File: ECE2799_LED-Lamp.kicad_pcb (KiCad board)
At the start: 2 copper layers, 138 x 46 mm, 91 parts, among them J1 IEC_60320_C8_Receptacle, J4 Conn_01x32, T1 750817251, U1 LT3799EMSE-PBF, U2 MP9989GV-Z, U3 LMR36006BRNXT, U4 FDMQ8205A, U5 140356145400, U6 140356145400, U7 RP2040, U8 CY8C20666A-24LQXI

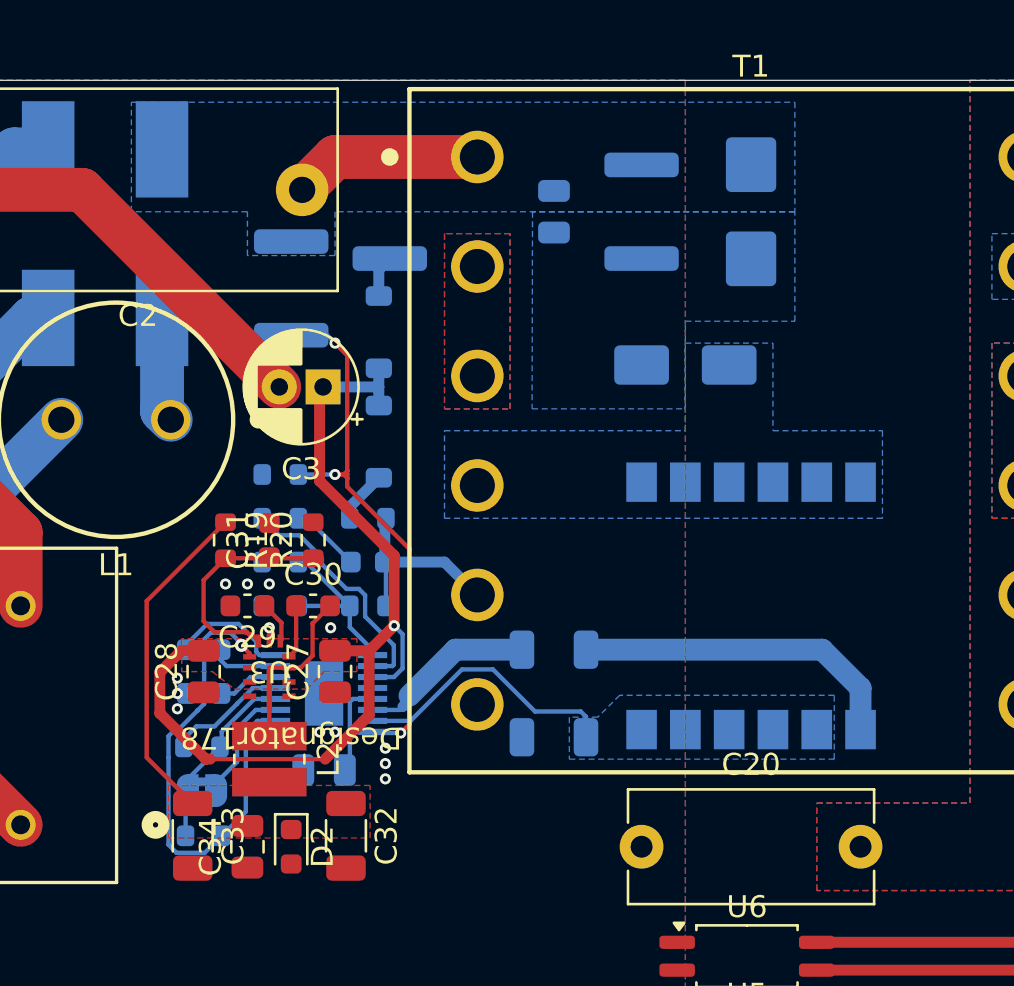
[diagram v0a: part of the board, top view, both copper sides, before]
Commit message: new FET
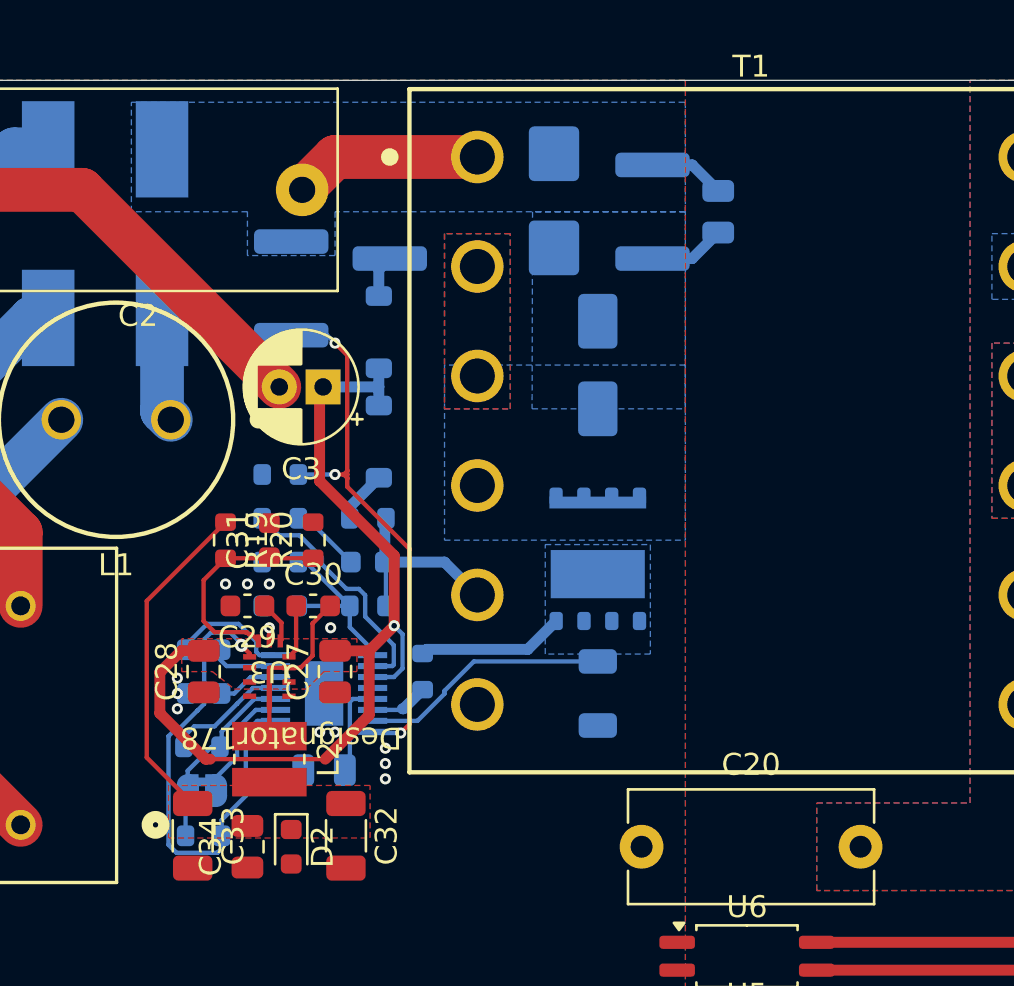
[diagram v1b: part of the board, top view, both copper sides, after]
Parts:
- C12, C14, C15, C16, C17: value C -> 100n
- C5: value C -> 1u
- Q1: value ~ -> IGLR65R200D2; footprint GAN039-650NTB:GAN039-650NTB -> PG-TSON-8-8:PG-TSON-8-8
- R25: footprint Resistor_SMD:R_1206_3216Metric -> Resistor_SMD:R_0603_1608Metric
- moved D3 9.01 mm to (151.0, 89.5)
- moved C13 7.50 mm to (158.5, 90.0)
- moved Q1 7.32 mm to (153.0, 105.8), turned to 90 degrees
- moved R25 6.08 mm to (145.0, 111.0), turned to 90 degrees
- moved D4 4.00 mm to (153.0, 97.0), turned to -90 degrees
- moved R8 2.83 mm to (153.0, 112.0), turned to -90 degrees
- moved R32 0.50 mm to (155.5, 90.0)
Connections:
- Q1 pad 1: /LED_Driver_AC-DC/GATE -> /LED_Driver_AC-DC/SENSE
- Q1 pad 4: /LED_Driver_AC-DC/SENSE -> /LED_Driver_AC-DC/GATE
- Q1 pad 5: /LED_Driver_AC-DC/SENSE -> /LED_Driver_AC-DC/DRAIN
- Q1 pad 6: /LED_Driver_AC-DC/SENSE -> /LED_Driver_AC-DC/DRAIN
- Q1 pad 9: /LED_Driver_AC-DC/DRAIN -> /LED_Driver_AC-DC/SENSE
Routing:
- net /LED_Driver_AC-DC/GATE: track 15.2 -> 6.72 mm
- net Net-(U1-GATE): track 8.08 -> 2.65 mm
- net /LED_Driver_AC-DC/FREEWHEEL: track 0.00 -> 3.49 mm
- net /LED_Driver_AC-DC/VHV: track 8.62 -> 12.1 mm
- net /LED_Driver_AC-DC/SENSE: track 12.6 -> 11.5 mm

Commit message: touch pcb
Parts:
- removed J4: Conn_01x32, Connector_FFC-FPC:Hirose_FH12-32S-0.5SH_1x32-1MP_P0.50mm_Horizontal
- added CS1: TRILL_BAR-26_CapSense, TRILL:TRILL_BAR_CapSense, F.Cu at (146.0, 140.0)
- added G5: OpenSourceHardware_Logo, TRILL:OpenSourceHardware_Logo, F.Cu at (95.5, 160.0)
- added J2: Conn_01x04_MountingPin, TRILL:qwiic_horizontal_SMD, B.Cu at (208.0, 145.0)
- moved C18 43.6 mm to (200.0, 138.0), turned to -90 degrees
- moved U8 41.1 mm to (200.0, 144.0)
- moved U7 0.40 mm to (217.0, 93.0), turned to 90 degrees
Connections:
- U8 pad 10: /Capacitive_Touch_Sensor/SENSE26 -> /Capacitive_Touch_Sensor/SENSE22
- U8 pad 11: /Capacitive_Touch_Sensor/SENSE27 -> /Capacitive_Touch_Sensor/SENSE23
- U8 pad 12: /Capacitive_Touch_Sensor/SENSE28 -> /Capacitive_Touch_Sensor/SENSE24
- U8 pad 13: /Capacitive_Touch_Sensor/SENSE29 -> /Capacitive_Touch_Sensor/SENSE25
- U8 pad 16: /Capacitive_Touch_Sensor/SENSE30 -> /Capacitive_Touch_Sensor/SENSE26
- U8 pad 2: /Capacitive_Touch_Sensor/SENSE18 -> unconnected-(U8-P2[7]-Pad2)
- U8 pad 3: /Capacitive_Touch_Sensor/SENSE19 -> unconnected-(U8-P2[5]-Pad3)
- U8 pad 4: /Capacitive_Touch_Sensor/SENSE20 -> unconnected-(U8-P2[3]-Pad4)
- U8 pad 5: /Capacitive_Touch_Sensor/SENSE21 -> unconnected-(U8-P2[1]-Pad5)
- U8 pad 6: /Capacitive_Touch_Sensor/SENSE22 -> /Capacitive_Touch_Sensor/SENSE18
- U8 pad 7: /Capacitive_Touch_Sensor/SENSE23 -> /Capacitive_Touch_Sensor/SENSE19
- U8 pad 8: /Capacitive_Touch_Sensor/SENSE24 -> /Capacitive_Touch_Sensor/SENSE20
- U8 pad 9: /Capacitive_Touch_Sensor/SENSE25 -> /Capacitive_Touch_Sensor/SENSE21
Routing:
- net /Capacitive_Touch_Sensor/SENSE1: track 0.00 -> 112.3 mm, vias 0 -> 1
- net /Capacitive_Touch_Sensor/SENSE2: track 0.00 -> 108.1 mm, vias 0 -> 1
- net /Capacitive_Touch_Sensor/SENSE3: track 0.00 -> 104.0 mm, vias 0 -> 1
- net /Capacitive_Touch_Sensor/SENSE4: track 0.00 -> 99.9 mm, vias 0 -> 1
- net /Capacitive_Touch_Sensor/SENSE5: track 0.00 -> 95.7 mm, vias 0 -> 1
- net /Capacitive_Touch_Sensor/SENSE6: track 0.00 -> 91.6 mm, vias 0 -> 1
- net /Capacitive_Touch_Sensor/SENSE7: track 0.00 -> 87.5 mm, vias 0 -> 1
- net /Capacitive_Touch_Sensor/SENSE8: track 0.00 -> 83.6 mm, vias 0 -> 1
- net /Capacitive_Touch_Sensor/SENSE9: track 0.00 -> 79.5 mm, vias 0 -> 1
- net /Capacitive_Touch_Sensor/SENSE10: track 0.00 -> 75.4 mm, vias 0 -> 1
- net /Capacitive_Touch_Sensor/SENSE11: track 0.00 -> 74.1 mm, vias 0 -> 1
- net /Capacitive_Touch_Sensor/SENSE12: track 0.00 -> 70.9 mm, vias 0 -> 1
- net /Capacitive_Touch_Sensor/SENSE13: track 0.00 -> 67.5 mm, vias 0 -> 1
- net /Capacitive_Touch_Sensor/SENSE14: track 0.00 -> 64.0 mm, vias 0 -> 1
- net /Capacitive_Touch_Sensor/SENSE15: track 0.00 -> 61.0 mm, vias 0 -> 1
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- added copper zone on B.Cu, net /Capacitive_Touch_Sensor/SENSE1
- added copper zone on B.Cu, net /Capacitive_Touch_Sensor/SENSE10
- added copper zone on B.Cu, net /Capacitive_Touch_Sensor/SENSE11
- added copper zone on B.Cu, net /Capacitive_Touch_Sensor/SENSE12
- added copper zone on B.Cu, net /Capacitive_Touch_Sensor/SENSE13
- added copper zone on B.Cu, net /Capacitive_Touch_Sensor/SENSE14
- added copper zone on B.Cu, net /Capacitive_Touch_Sensor/SENSE15
- added copper zone on B.Cu, net /Capacitive_Touch_Sensor/SENSE16
- added copper zone on B.Cu, net /Capacitive_Touch_Sensor/SENSE17
- added copper zone on B.Cu, net /Capacitive_Touch_Sensor/SENSE18
- added copper zone on B.Cu, net /Capacitive_Touch_Sensor/SENSE19
- added copper zone on B.Cu, net /Capacitive_Touch_Sensor/SENSE2
- added copper zone on B.Cu, net /Capacitive_Touch_Sensor/SENSE20
- added copper zone on B.Cu, net /Capacitive_Touch_Sensor/SENSE21
- added copper zone on B.Cu, net /Capacitive_Touch_Sensor/SENSE22
- added copper zone on B.Cu, net /Capacitive_Touch_Sensor/SENSE23
- added copper zone on B.Cu, net /Capacitive_Touch_Sensor/SENSE24
- added copper zone on B.Cu, net /Capacitive_Touch_Sensor/SENSE25
- added copper zone on B.Cu, net /Capacitive_Touch_Sensor/SENSE26
- added copper zone on B.Cu, net /Capacitive_Touch_Sensor/SENSE3
- added copper zone on B.Cu, net /Capacitive_Touch_Sensor/SENSE4
- added copper zone on B.Cu, net /Capacitive_Touch_Sensor/SENSE5
- added copper zone on B.Cu, net /Capacitive_Touch_Sensor/SENSE6
- added copper zone on B.Cu, net /Capacitive_Touch_Sensor/SENSE7
- added copper zone on B.Cu, net /Capacitive_Touch_Sensor/SENSE8
- added copper zone on B.Cu, net /Capacitive_Touch_Sensor/SENSE9
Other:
- board size 138 x 46 mm -> 116 x 72 mm

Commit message: updated components
New ganfet selected and further work developing the rp2040 microcontroller circuit
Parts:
- removed H1: MountingHole_Pad, MountingHole:MountingHole_3.2mm_M3_Pad
- added C22: 100n, Capacitor_SMD:C_0603_1608Metric, F.Cu at (234.2, 90.0)
- added C24: 100n, Capacitor_SMD:C_0603_1608Metric, F.Cu at (234.2, 92.5)
- added C25: 100n, Capacitor_SMD:C_0603_1608Metric, F.Cu at (234.2, 95.0)
- added C26: 33p, Capacitor_SMD:C_0603_1608Metric, F.Cu at (215.7, 70.4)
- added C35: 33p, Capacitor_SMD:C_0603_1608Metric, F.Cu at (215.7, 72.9)
- added C36: C, Capacitor_SMD:C_0603_1608Metric, F.Cu at (215.7, 75.4)
- added C37: C, Capacitor_SMD:C_0603_1608Metric, F.Cu at (215.7, 77.9)
- added J3: Conn_ARM_SWD_TagConnect_TC2030-NL, Connector:Tag-Connect_TC2030-IDC-NL_2x03_P1.27mm_Vertical, F.Cu at (228.2, 91.2)
- added J4: Conn_01x02_Pin, Connector_PinHeader_2.54mm:PinHeader_1x02_P2.54mm_Vertical, F.Cu at (250.0, 97.5)
- added J5: Conn_01x04_MountingPin, TRILL:qwiic_horizontal_SMD, F.Cu at (241.2, 100.2)
- added JP1: SolderJumper_2_Bridged, Jumper:SolderJumper-2_P1.3mm_Bridged2Bar_RoundedPad1.0x1.5mm, F.Cu at (227.8, 79.0)
- added R28: 0, Resistor_SMD:R_0603_1608Metric, F.Cu at (215.7, 80.4)
- added R29: 1k, Resistor_SMD:R_0603_1608Metric, F.Cu at (215.7, 82.9)
- added R30: 100, Resistor_SMD:R_0603_1608Metric, F.Cu at (219.7, 70.4)
- added R31: 100, Resistor_SMD:R_0603_1608Metric, F.Cu at (219.7, 72.9)
- added R33: 1k, Resistor_SMD:R_0603_1608Metric, F.Cu at (219.7, 75.4)
- added R34: 27.4, Resistor_SMD:R_0603_1608Metric, F.Cu at (219.7, 77.9)
- added R35: 27.4, Resistor_SMD:R_0603_1608Metric, F.Cu at (219.7, 80.4)
- added R36: R, Resistor_SMD:R_0603_1608Metric, F.Cu at (219.7, 82.9)
- added R37: R, Resistor_SMD:R_0603_1608Metric, F.Cu at (223.7, 70.4)
- added R38: R, Resistor_SMD:R_0603_1608Metric, F.Cu at (223.7, 72.9)
- added R39: 4.7k, Resistor_SMD:R_0603_1608Metric, F.Cu at (223.7, 75.4)
- added R40: 4.7k, Resistor_SMD:R_0603_1608Metric, F.Cu at (223.7, 77.9)
- added TP1: TestPoint, TestPoint:TestPoint_Pad_D2.0mm, F.Cu at (227.7, 71.2)
- added TP2: TestPoint, TestPoint:TestPoint_Pad_D2.0mm, F.Cu at (227.7, 75.2)
- added U9: AT25xxx, Package_SO:SOIC-8_3.9x4.9mm_P1.27mm, F.Cu at (228.4, 85.5)
- added Y1: 830070868, Crystal:Crystal_SMD_3225-4Pin_3.2x2.5mm, F.Cu at (235.2, 84.4)
- C15: value 100n -> 1u
- J1: value IEC_60320_C8_Receptacle -> IEC_60320_C6_Receptacle; footprint RAPC322X:SWITCHCRAFT_RAPC322X -> IEC_60320_C6:IEC_60320_C6
- J2: moved to F.Cu
- moved G5 98.8 mm to (193.0, 144.0)
- moved C19 50.9 mm to (202.0, 150.0), turned to 180 degrees
- moved R21 48.9 mm to (208.0, 149.0), turned to 0 degrees
- moved R17 39.7 mm to (208.0, 139.0), turned to 0 degrees
- moved JP3 38.2 mm to (207.0, 135.0), turned to 90 degrees
- moved RV1 36.9 mm to (106.8, 124.5), turned to 180 degrees
- moved JP4 33.3 mm to (210.0, 135.0), turned to 90 degrees
- moved R22 32.4 mm to (205.0, 134.0), turned to 90 degrees
- moved R24 26.6 mm to (212.0, 134.0), turned to 90 degrees
- moved J1 9.85 mm to (94.0, 107.0)
- moved J2 2.60 mm to (210.4, 144.0), turned to 90 degrees
- moved FL1 1.85 mm to (128.5, 118.0)
- moved C1 1.50 mm to (113.5, 100.0)
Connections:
- net Net-(U7-VREG_VOUT) renamed +1V1
- C18 pad 1: GND -> GND1
- C18 pad 2: +3V3 -> VCC
- C19 pad 2: GND -> GND1
- C2 pad 2: GND -> GNDPWR
- C20 pad 1: GND -> GNDPWR
- C27 pad 1: GND -> GNDPWR
- C28 pad 1: GND -> GNDPWR
- C29 pad 2: GND -> GNDPWR
- C3 pad 2: GND -> GNDPWR
- C31 pad 2: GND -> GNDPWR
- C32 pad 2: GND -> GNDPWR
- C33 pad 2: GND -> GNDPWR
- C34 pad 1: GND -> GNDPWR
- C7 pad 2: GND -> GNDPWR
- C8 pad 1: GND -> GNDPWR
- C9 pad 1: GND -> GNDPWR
- D1 pad 4: GND -> GNDPWR
- D2 pad 2: GND -> GNDPWR
- J2 pad 1: GND -> GND1
- J2 pad 2: +3V3 -> VCC
- J2 pad MP: GND -> GND1
- JP3 pad 1: +3V3 -> VCC
- JP3 pad 3: GND -> GND1
- JP4 pad 1: unconnected-(JP4-A-Pad1) -> VCC
- JP4 pad 3: GND -> GND1
- R20 pad 2: GND -> GNDPWR
- R22 pad 2: GND -> GND1
- R23 pad 2: GND -> GNDPWR
- R24 pad 2: GND -> GND1
- R4 pad 1: GND -> GNDPWR
- R8 pad 2: GND -> GNDPWR
- T1 pad 6: GND -> GNDPWR
- U1 pad EPAD: GND -> GNDPWR
- U3 pad 1: GND -> GNDPWR
- U3 pad 11: GND -> GNDPWR
- U3 pad 6: GND -> GNDPWR
- U7 pad 19: unconnected-(U7-TESTEN-Pad19) -> GND
- U7 pad 2: unconnected-(U7-GPIO0-Pad2) -> /Microcontroller/SDA
- U7 pad 20: unconnected-(U7-XIN-Pad20) -> /Microcontroller/XIN
- U7 pad 21: unconnected-(U7-XOUT-Pad21) -> /Microcontroller/XOUT
- U7 pad 24: unconnected-(U7-SWCLK-Pad24) -> /Microcontroller/SWCLK
- U7 pad 25: unconnected-(U7-SWD-Pad25) -> /Microcontroller/SWDIO
- U7 pad 26: unconnected-(U7-RUN-Pad26) -> +3V3
- U7 pad 3: unconnected-(U7-GPIO1-Pad3) -> /Microcontroller/SCL
- U7 pad 38: unconnected-(U7-GPIO26_ADC0-Pad38) -> /Microcontroller/TEMP_SENSE
- U7 pad 4: unconnected-(U7-GPIO2-Pad4) -> /Microcontroller/PWM_DIM
- U7 pad 46: unconnected-(U7-USB_DM-Pad46) -> /Microcontroller/USB_DM
- U7 pad 47: unconnected-(U7-USB_DP-Pad47) -> /Microcontroller/USB_DP
- U7 pad 5: unconnected-(U7-GPIO3-Pad5) -> /~{FAULT}
- U7 pad 51: unconnected-(U7-QSPI_SD3-Pad51) -> /Microcontroller/QSPI_IO3
- U7 pad 52: unconnected-(U7-QSPI_SCLK-Pad52) -> /Microcontroller/QSPI_CLK
- U7 pad 53: unconnected-(U7-QSPI_SD0-Pad53) -> /Microcontroller/QSPI_IO0
- U7 pad 54: unconnected-(U7-QSPI_SD2-Pad54) -> /Microcontroller/QSPI_IO2
- U7 pad 55: unconnected-(U7-QSPI_SD1-Pad55) -> /Microcontroller/QSPI_IO1
- U7 pad 56: unconnected-(U7-QSPI_SS-Pad56) -> /Microcontroller/QSPI_~{CS}
- U7 pad 6: unconnected-(U7-GPIO4-Pad6) -> /DIR_A
- U7 pad 7: unconnected-(U7-GPIO5-Pad7) -> /DIR_B
- U8 pad 18: GND -> GND1
- U8 pad 21: +3V3 -> VCC
- U8 pad 25: /Capacitive_Touch_Sensor/EVENT -> unconnected-(U8-P1[6]-Pad25)
- U8 pad 26: /Capacitive_Touch_Sensor/XRES -> unconnected-(U8-XRES-Pad26)
- U8 pad 41: +3V3 -> VCC
- U8 pad 47: GND -> GND1
- U8 pad 49: GND -> GND1
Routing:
- net VCC: track 0.00 -> 41.5 mm, vias 0 -> 4
- net GNDPWR: track 0.00 -> 22.7 mm, vias 0 -> 41
- net GND: track 22.7 -> 0.00 mm, vias 13 -> 0
- net Net-(U8-(PR/SDA)P1[0]): track 1.22 -> 22.8 mm, vias 0 -> 2
- net /Capacitive_Touch_Sensor/ADDR1: track 2.17 -> 20.2 mm, vias 1 -> 2
- net /AC-: track 50.1 -> 33.7 mm
- net /Capacitive_Touch_Sensor/ADDR0: track 2.17 -> 14.5 mm, vias 1 -> 2
- net /AC+: track 43.8 -> 32.9 mm
- net Net-(U8-(PR/SCL)P1[1]): track 0.00 -> 9.41 mm, vias 0 -> 2
- net GND1: track 0.00 -> 8.75 mm, vias 0 -> 29
- net /Capacitive_Touch_Sensor/SDA: track 0.00 -> 6.59 mm
- net /Capacitive_Touch_Sensor/SCL: track 0.00 -> 3.76 mm
- net Net-(U8-(INT)P0[1]): track 0.00 -> 3.29 mm
- net /Capacitive_Touch_Sensor/SENSE26: track 10.5 -> 11.1 mm
- added copper zone on B.Cu, net GND1
- added copper zone on F.Cu, net GND1
- added copper zone on B.Cu, net GNDPWR
- added copper zone on F.Cu, net GNDPWR
- removed copper zone on B.Cu, net GND
- removed copper zone on F.Cu, net GND
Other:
- board size 116 x 72 mm -> 119 x 72 mm

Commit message: board routing progress
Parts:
- J5, U7: moved to B.Cu
- moved Y1 98.3 mm to (149.0, 131.5)
- moved J3 94.1 mm to (141.0, 126.5), turned to -90 degrees
- moved J5 90.2 mm to (155.1, 126.9), turned to 180 degrees
- moved U9 89.6 mm to (148.5, 126.0), turned to -90 degrees
- moved U7 76.8 mm to (147.0, 124.5), turned to -90 degrees
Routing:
- net GNDPWR: vias 41 -> 35

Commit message: full layout
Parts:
- removed C14: 100n, Capacitor_SMD:C_0603_1608Metric
- added S1: 435171014816, 435171014816:435171014816, F.Cu at (137.0, 126.5)
- C26, C35, C36, C37, R28, R29, R36, R37, TP1, TP2, U9, Y1: moved to B.Cu
- J5: moved to F.Cu
- moved J4 132.8 mm to (120.7, 128.0), turned to 90 degrees
- moved TP1 114.7 mm to (127.5, 127.0), turned to 90 degrees
- moved TP2 108.8 mm to (132.0, 127.0), turned to 90 degrees
- moved C25 104.6 mm to (134.5, 126.5), turned to 90 degrees
- moved C22 97.8 mm to (143.5, 126.5)
- moved R39 96.8 mm to (140.5, 125.0), turned to 180 degrees
- moved C24 95.9 mm to (143.5, 123.5)
- moved R33 95.2 mm to (137.5, 123.5), turned to 180 degrees
- moved R40 94.8 mm to (140.5, 123.5), turned to 180 degrees
- moved R38 94.8 mm to (146.5, 128.0), turned to 180 degrees
- moved R34 92.9 mm to (140.5, 126.5), turned to 180 degrees
- moved JP1 92.8 mm to (149.4, 128.5), turned to 180 degrees
- moved R37 92.4 mm to (144.5, 118.0)
- moved R35 92.4 mm to (140.5, 128.0)
- moved R30 88.9 mm to (149.5, 125.0), turned to 180 degrees
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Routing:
- net /~{FAULT}: track 5.58 -> 32.7 mm
- net /Microcontroller/TEMP_SENSE: track 0.00 -> 24.7 mm
- net +3V3: track 15.2 -> 39.4 mm, vias 0 -> 7
- net /DIM: track 0.00 -> 16.8 mm
- net /Microcontroller/USB_DP_in: track 0.00 -> 16.1 mm, vias 0 -> 1
- net Net-(R15-Pad2): track 0.00 -> 13.7 mm
- net /Microcontroller/USB_DM_in: track 0.00 -> 11.4 mm, vias 0 -> 1
- net /Microcontroller/QSPI_IO3: track 0.00 -> 11.3 mm
- net +1V1: track 0.00 -> 11.0 mm, vias 0 -> 2
- net /Microcontroller/QSPI_CLK: track 0.00 -> 9.91 mm
- net /Microcontroller/QSPI_~{CS}: track 0.00 -> 9.11 mm
- net /Microcontroller/QSPI_IO1: track 0.00 -> 7.71 mm
- net Net-(R16-Pad1): track 0.00 -> 7.49 mm
- net /Microcontroller/QSPI_IO0: track 0.00 -> 6.60 mm
- net /Microcontroller/SCL: track 0.00 -> 6.55 mm, vias 0 -> 1
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- added copper zone on B.Cu, net GND
- added copper zone on F.Cu, net GND

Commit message: finished board
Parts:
- removed C13: 1.5n, Capacitor_SMD:C_0805_2012Metric
- removed JP1: SolderJumper_2_Bridged, Jumper:SolderJumper-2_P1.3mm_Bridged2Bar_RoundedPad1.0x1.5mm
- added J6: Conn_01x02, Connector_Wire:SolderWire-0.75sqmm_1x02_P4.8mm_D1.25mm_OD2.3mm, F.Cu at (198.0, 102.4)
- R38: moved to B.Cu
- moved R38 21.5 mm to (125.0, 128.0), turned to -90 degrees
- moved C11 2.00 mm to (186.3, 109.0)
- moved J2 1.08 mm to (210.0, 143.0)
- moved C18 1.00 mm to (200.0, 137.0)
- moved C19 1.00 mm to (202.0, 149.0)
- moved CS1 1.00 mm to (146.0, 139.0)
- moved D10 1.00 mm to (191.0, 95.0)
- moved D11 1.00 mm to (195.0, 95.0)
- moved D12 1.00 mm to (193.0, 108.0)
- moved D13 1.00 mm to (193.0, 92.0)
- moved D6 1.00 mm to (191.0, 105.0)
- moved D7 1.00 mm to (195.0, 105.0)
- moved G5 1.00 mm to (193.0, 143.0)
- moved JP3 1.00 mm to (207.0, 134.0)
- moved JP4 1.00 mm to (210.0, 134.0)
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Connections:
- J3 pad 1: /Microcontroller/3V3_in -> +3V3
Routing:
- net +3V3: track 39.4 -> 106.1 mm, vias 7 -> 10
- net /Microcontroller/SDA: track 6.18 -> 23.1 mm
- net /Microcontroller/SCL: track 6.55 -> 22.3 mm
- net GND: track 0.00 -> 10.6 mm, vias 0 -> 37
- net /Microcontroller/3V3_in: track 5.85 -> 0.00 mm
- net Net-(R33-Pad1): track 0.00 -> 4.69 mm
- net /LED_Driver_AC-DC/FREEWHEEL: track 3.49 -> 0.00 mm
- net /LED_Driver_AC-DC/VHV: track 12.1 -> 8.62 mm
- net /Microcontroller/QSPI_~{CS}: track 9.11 -> 12.3 mm, vias 0 -> 1
- net Net-(R15-Pad2): track 13.7 -> 10.7 mm
- net Net-(R16-Pad1): track 7.49 -> 10.2 mm
- net /LED_B: track 5.28 -> 6.86 mm
- net /LED_A: track 5.28 -> 6.86 mm
- net Net-(D10-K): track 53.3 -> 53.8 mm
- net GNDPWR: vias 70 -> 73
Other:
- board size 119 x 72 mm -> 119 x 71 mm
